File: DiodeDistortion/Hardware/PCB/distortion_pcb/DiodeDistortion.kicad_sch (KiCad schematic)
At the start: 24 parts, among them J1 THONKICONN, J2 THONKICONN, J3 THONKICONN, J4 Conn_01x10_Pin, U1 TL074, U2 NSL-32

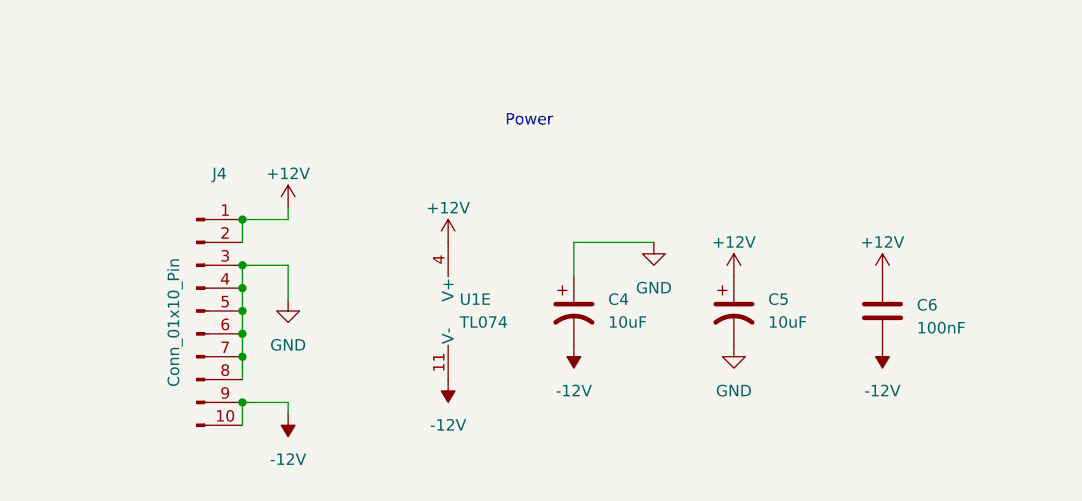
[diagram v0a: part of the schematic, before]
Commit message: post-processed faceplate for kicad import and added distortion faceplate
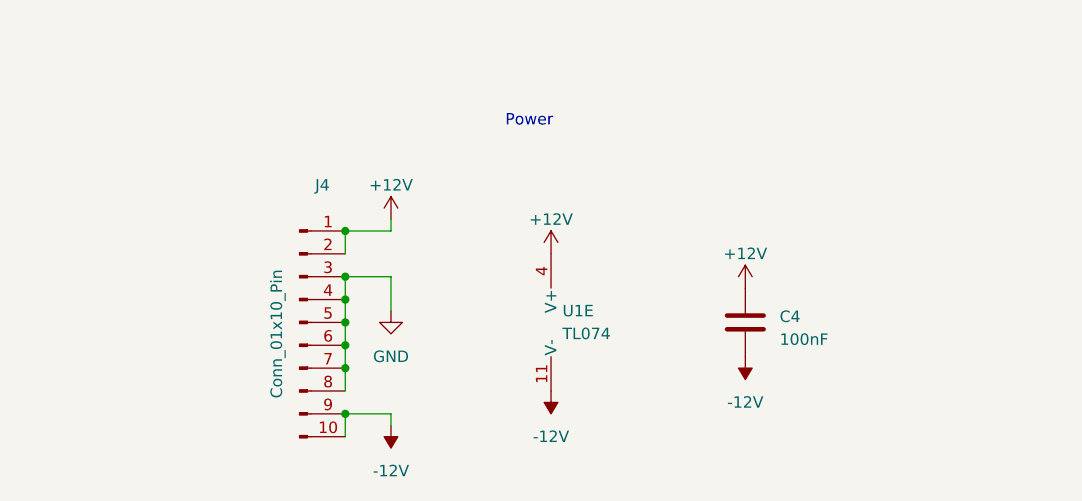
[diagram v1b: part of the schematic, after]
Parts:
- removed C4, C5: 10uF, Capacitor_THT:CP_Radial_D4.0mm_P2.00mm, symbol Device:C_Polarized_US
- renumbered C6 to C4
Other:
- moved on the sheet: C4, J4, U1E
